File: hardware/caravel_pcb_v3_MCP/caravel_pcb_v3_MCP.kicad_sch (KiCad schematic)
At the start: 38 parts, among them J1 USB_B_Micro - 10118193-0001LF, J2 Conn_01x14_Female, J3 Conn_01x02_Male, J4 Conn_01x02_Male, J5 Conn_01x02_Male, J6 Conn_01x02_Male, J7 Conn_01x06_Female, SW1 SW_Push - SKQGADE010, U1 MCP2221AxML, U2 AZ1117CH-1.8TRG1, U3 AZ1117-3.3, U4 caravel_breakout, U5 W25Q32FVSS, X1 DSC6001_10MHZ

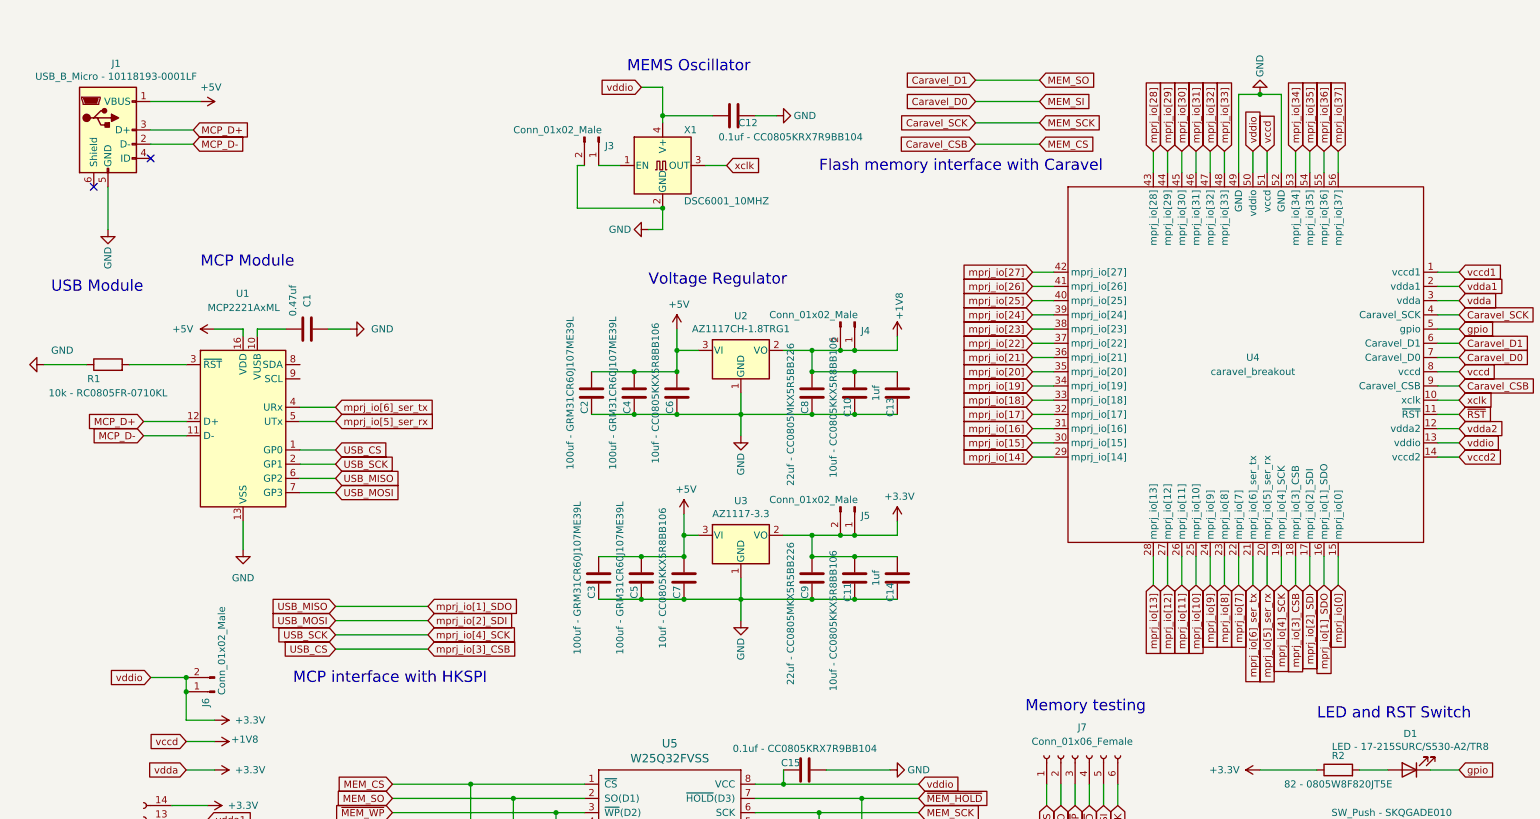
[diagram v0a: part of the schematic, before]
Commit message: Update MCP version of the V3 caravel board
Updates footprint assignments and create initial PCB.

Signed-off-by: Michael Welling <mwelling@ieee.org>
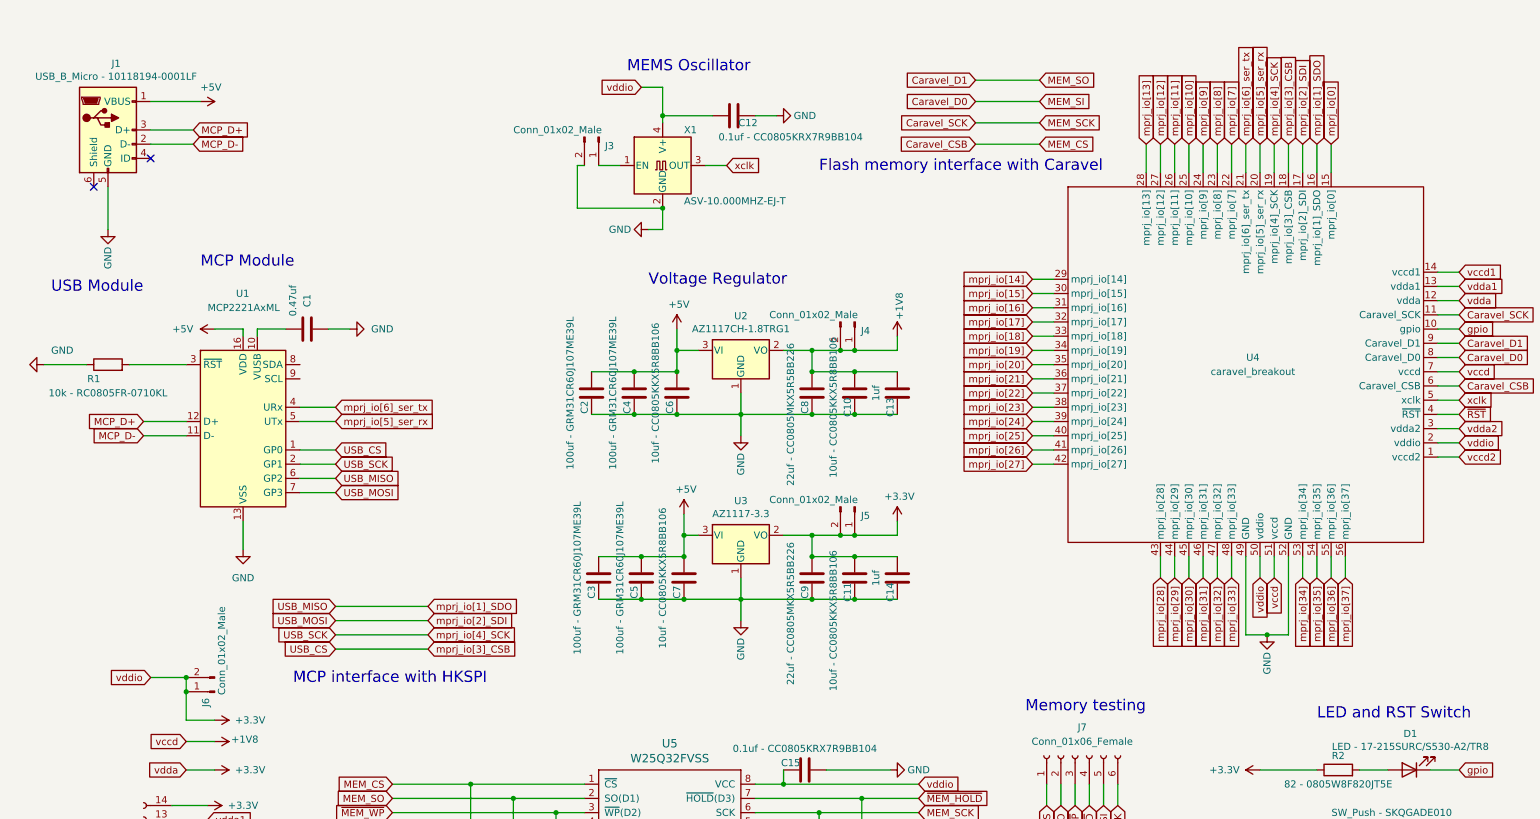
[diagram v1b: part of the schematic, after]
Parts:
- J1: value USB_B_Micro - 10118193-0001LF -> USB_B_Micro - 10118194-0001LF; footprint striVe_foot_prints:FCI_10118193-0001LF -> Connector_USB:USB_Micro-B_Amphenol_10118194_Horizontal
- J7: footprint (none) -> Connector_PinSocket_2.54mm:PinSocket_1x06_P2.54mm_Vertical
- SW1: footprint striVe_foot_prints:SW4-SMD-5.2X5.2X1.5MM -> Button_Switch_SMD:SW_SPST_SKQG_WithStem
- U2, U3: footprint Package_TO_SOT_SMD:SOT-223 -> Package_TO_SOT_SMD:SOT-223-3_TabPin2
- U4: footprint Caravel_Baord:caravel_breakout -> Caravel_Board:caravel_breakout_v1
- U5: footprint striVe_foot_prints:SOIC127P790X216-8N -> Package_SO:SOIC-8_5.23x5.23mm_P1.27mm
- X1: value DSC6001_10MHZ -> ASV-10.000MHZ-EJ-T; footprint striVe_foot_prints:DSC6001JE1A-010.0000 -> Oscillator:Oscillator_SMD_Abracon_ASV-4Pin_7.0x5.1mm
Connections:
- net +1V8: now also U4.7 (vccd); no longer U4.8 (vccd)
- net +3V3: now also U4.12 (vdda), U4.2 (vddio); no longer U4.13 (vddio), U4.3 (vdda)
- net Caravel_CSB: now also U4.6 (Caravel_CSB); no longer U4.9 (Caravel_CSB)
- net Caravel_D0: now also U4.8 (Caravel_D0); no longer U4.7 (Caravel_D0)
- net Caravel_D1: now also U4.9 (Caravel_D1); no longer U4.6 (Caravel_D1)
- net Caravel_SCK: now also U4.11 (Caravel_SCK); no longer U4.4 (Caravel_SCK)
- net gpio: now also U4.10 (gpio); no longer U4.5 (gpio)
- net vccd1: now also U4.14 (vccd1); no longer U4.1 (vccd1)
- net vccd2: now also U4.1 (vccd2); no longer U4.14 (vccd2)
- net vdda1: now also U4.13 (vdda1); no longer U4.2 (vdda1)
- net vdda2: now also U4.3 (vdda2); no longer U4.12 (vdda2)
- net xclk: now also U4.5 (xclk); no longer U4.10 (xclk)
- net ~{RST}: now also U4.4 (~{RST}); no longer U4.11 (~{RST})

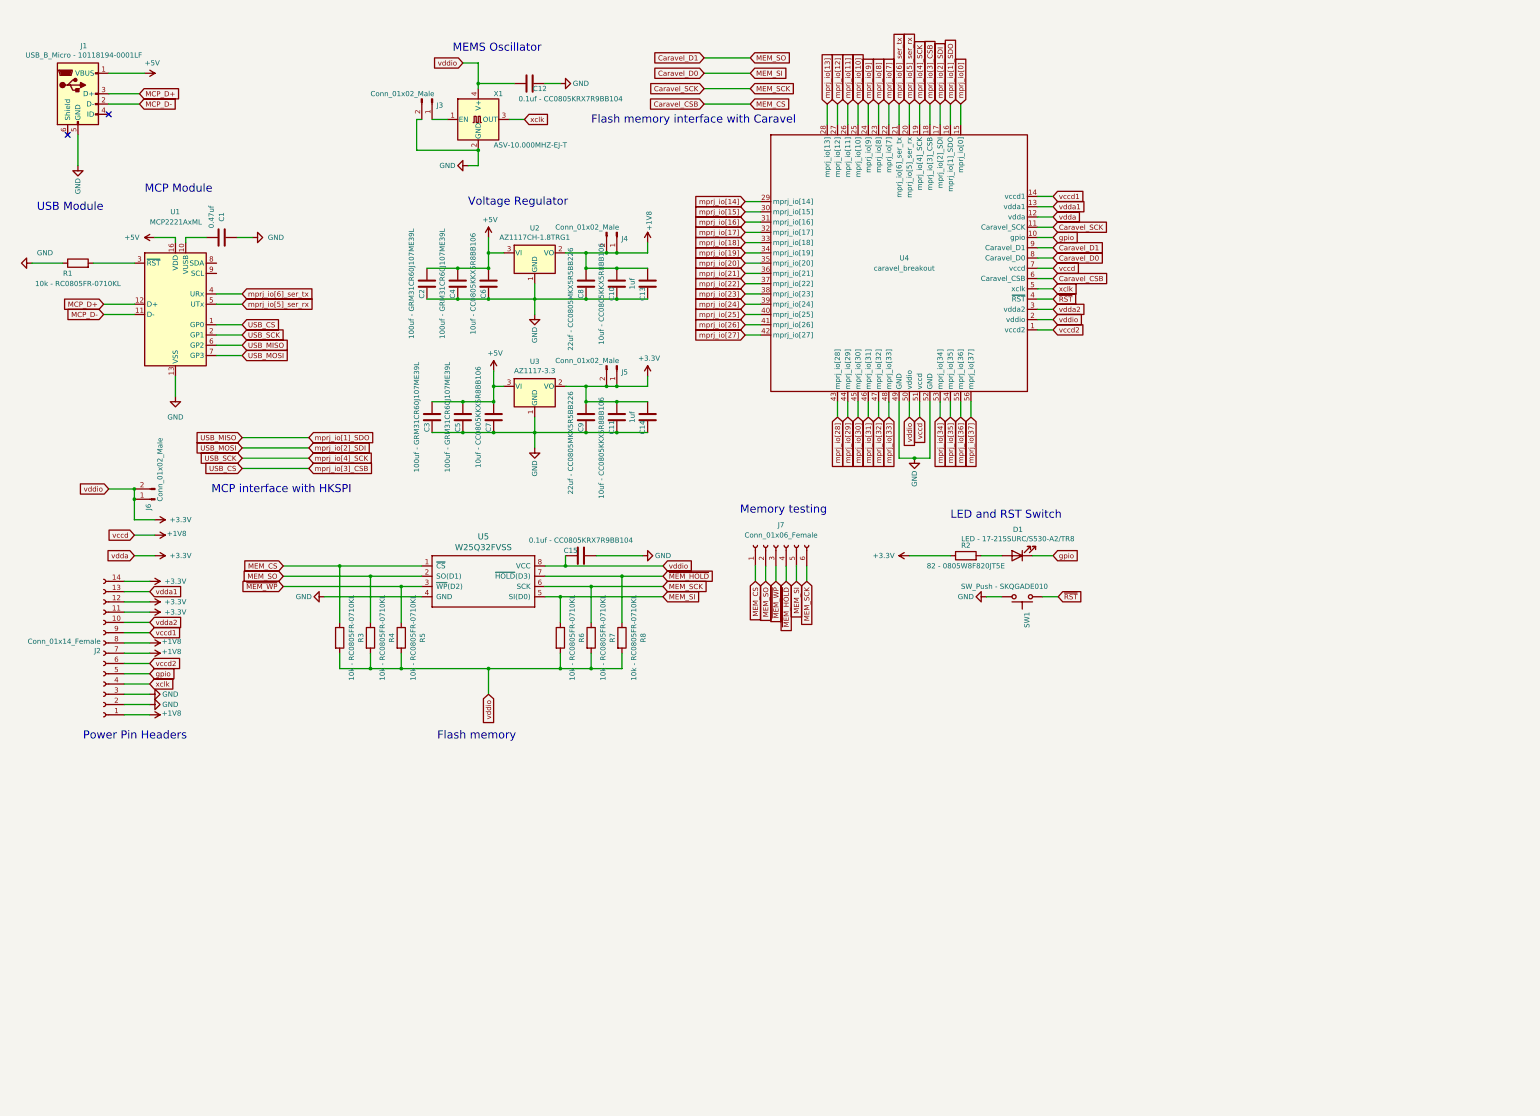
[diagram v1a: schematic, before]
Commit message: update caravel breakout symbol in schematic
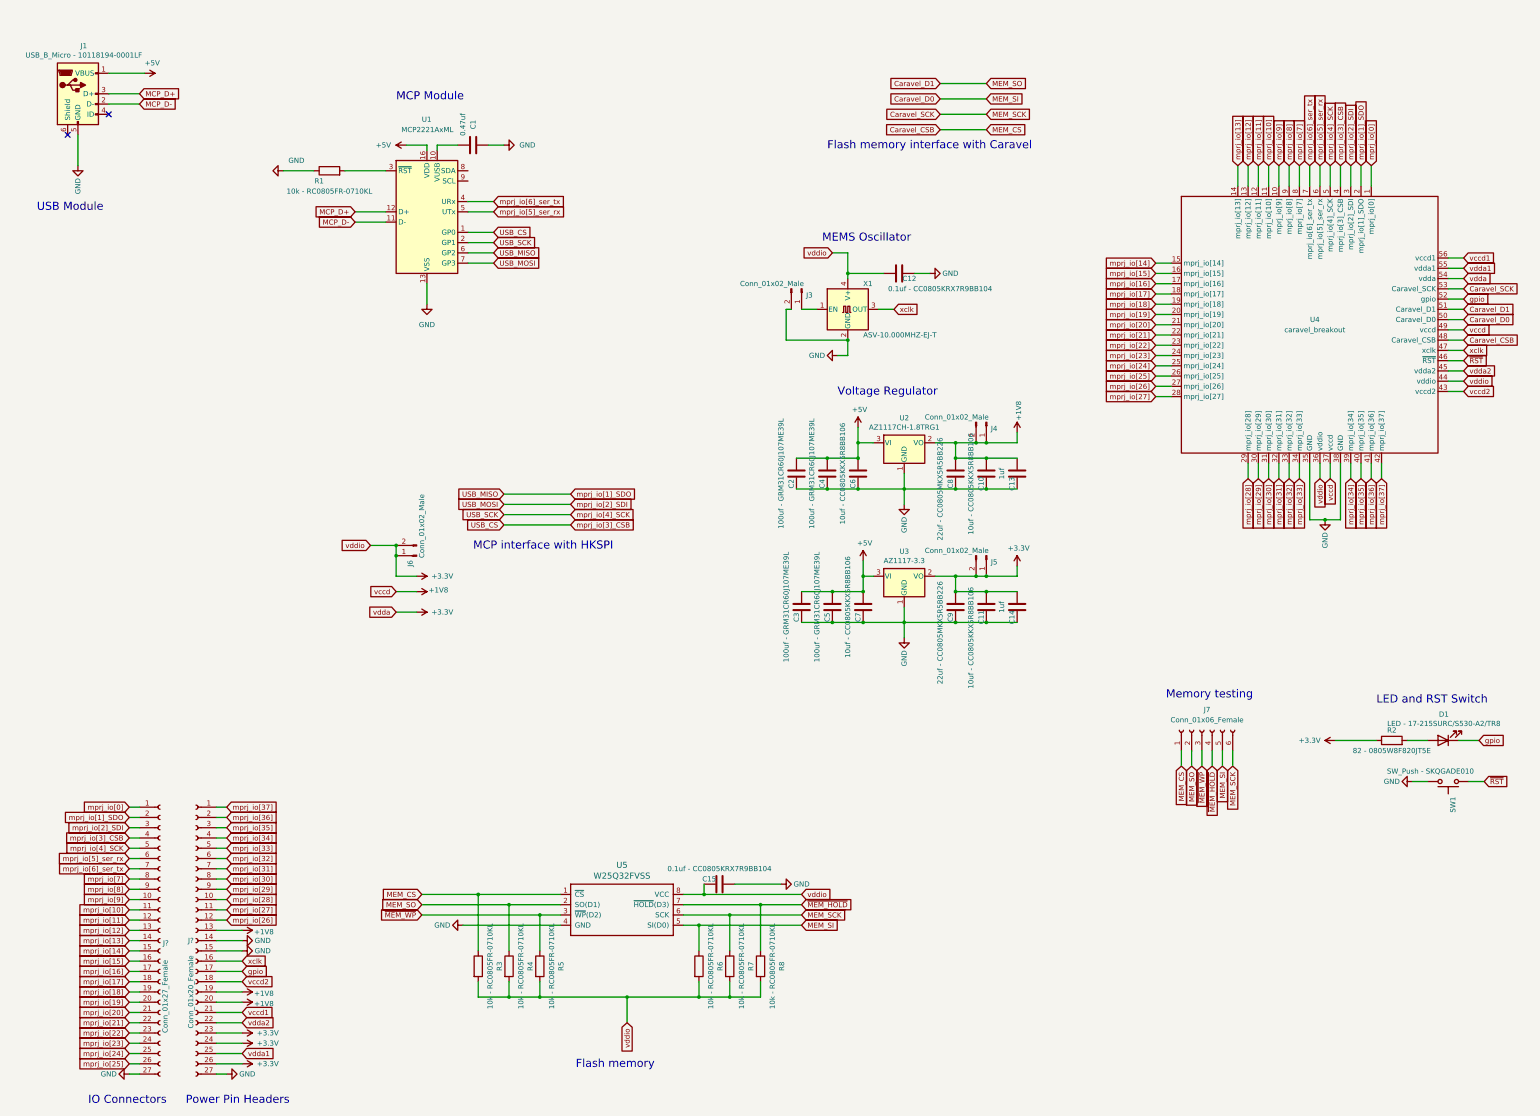
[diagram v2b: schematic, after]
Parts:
- removed J2: Conn_01x14_Female, Connector_PinHeader_2.54mm:PinHeader_1x14_P2.54mm_Vertical, symbol Connector:Conn_01x14_Female
- added J?: Conn_01x27_Female, Connector_PinHeader_2.54mm:PinHeader_1x27_P2.54mm_Vertical, symbol Connector:Conn_01x27_Female
- added J?: Conn_01x20_Female, Connector_PinHeader_2.54mm:PinHeader_1x20_P2.54mm_Vertical, symbol Connector:Conn_01x27_Female
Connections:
- net +1V8: now also U4.37 (vccd), U4.49 (vccd), J?.13 (Pin_13), J?.19 (Pin_19), J?.20 (Pin_20); no longer U4.51 (vccd), U4.7 (vccd)
- net +3V3: now also U4.36 (vddio), U4.44 (vddio), U4.54 (vdda), J?.23 (Pin_23), J?.24 (Pin_24), J?.26 (Pin_26); no longer U4.12 (vdda), U4.2 (vddio), U4.50 (vddio)
- net Caravel_CSB: now also U4.48 (Caravel_CSB); no longer U4.6 (Caravel_CSB)
- net Caravel_D0: now also U4.50 (Caravel_D0); no longer U4.8 (Caravel_D0)
- net Caravel_D1: now also U4.51 (Caravel_D1); no longer U4.9 (Caravel_D1)
- net Caravel_SCK: now also U4.53 (Caravel_SCK); no longer U4.11 (Caravel_SCK)
- net GND: now also U4.35 (GND), U4.38 (GND), J?.14 (Pin_14), J?.15 (Pin_15), J?.27 (Pin_27), J?.27 (Pin_27); no longer U4.49 (GND), U4.52 (GND)
- net USB_CS: now also U4.4 (mprj_io[3]_CSB), J?.4 (Pin_4); no longer U4.18 (mprj_io[3]_CSB)
- net USB_MISO: now also U4.2 (mprj_io[1]_SDO), J?.2 (Pin_2); no longer U4.16 (mprj_io[1]_SDO)
- net USB_MOSI: now also U4.3 (mprj_io[2]_SDI), J?.3 (Pin_3); no longer U4.17 (mprj_io[2]_SDI)
- net USB_SCK: now also U4.5 (mprj_io[4]_SCK), J?.5 (Pin_5); no longer U4.19 (mprj_io[4]_SCK)
- net gpio: now also U4.52 (gpio), J?.17 (Pin_17); no longer U4.10 (gpio)
- net mprj_io[0]: now also U4.1 (mprj_io[0]), J?.1 (Pin_1); no longer U4.15 (mprj_io[0])
- net mprj_io[10]: now also U4.11 (mprj_io[10]), J?.11 (Pin_11); no longer U4.25 (mprj_io[10])
- net mprj_io[11]: now also U4.12 (mprj_io[11]), J?.12 (Pin_12); no longer U4.26 (mprj_io[11])
- net mprj_io[12]: now also U4.13 (mprj_io[12]), J?.13 (Pin_13); no longer U4.27 (mprj_io[12])
- net mprj_io[13]: now also U4.14 (mprj_io[13]), J?.14 (Pin_14); no longer U4.28 (mprj_io[13])
- net mprj_io[14]: now also U4.15 (mprj_io[14]), J?.15 (Pin_15); no longer U4.29 (mprj_io[14])
- net mprj_io[15]: now also U4.16 (mprj_io[15]), J?.16 (Pin_16); no longer U4.30 (mprj_io[15])
- net mprj_io[16]: now also U4.17 (mprj_io[16]), J?.17 (Pin_17); no longer U4.31 (mprj_io[16])
- net mprj_io[17]: now also U4.18 (mprj_io[17]), J?.18 (Pin_18); no longer U4.32 (mprj_io[17])
- net mprj_io[18]: now also U4.19 (mprj_io[18]), J?.19 (Pin_19); no longer U4.33 (mprj_io[18])
- net mprj_io[19]: now also U4.20 (mprj_io[19]), J?.20 (Pin_20); no longer U4.34 (mprj_io[19])
- net mprj_io[20]: now also U4.21 (mprj_io[20]), J?.21 (Pin_21); no longer U4.35 (mprj_io[20])
- net mprj_io[21]: now also U4.22 (mprj_io[21]), J?.22 (Pin_22); no longer U4.36 (mprj_io[21])
- net mprj_io[22]: now also U4.23 (mprj_io[22]), J?.23 (Pin_23); no longer U4.37 (mprj_io[22])
- net mprj_io[23]: now also U4.24 (mprj_io[23]), J?.24 (Pin_24); no longer U4.38 (mprj_io[23])
- net mprj_io[24]: now also U4.25 (mprj_io[24]), J?.25 (Pin_25); no longer U4.39 (mprj_io[24])
- net mprj_io[25]: now also U4.26 (mprj_io[25]), J?.26 (Pin_26); no longer U4.40 (mprj_io[25])
- net mprj_io[26]: now also U4.27 (mprj_io[26]), J?.12 (Pin_12); no longer U4.41 (mprj_io[26])
- net mprj_io[27]: now also U4.28 (mprj_io[27]), J?.11 (Pin_11); no longer U4.42 (mprj_io[27])
- net mprj_io[28]: now also U4.29 (mprj_io[28]), J?.10 (Pin_10); no longer U4.43 (mprj_io[28])
- net mprj_io[29]: now also U4.30 (mprj_io[29]), J?.9 (Pin_9); no longer U4.44 (mprj_io[29])
- net mprj_io[30]: now also U4.31 (mprj_io[30]), J?.8 (Pin_8); no longer U4.45 (mprj_io[30])
- net mprj_io[31]: now also U4.32 (mprj_io[31]), J?.7 (Pin_7); no longer U4.46 (mprj_io[31])
- net mprj_io[32]: now also U4.33 (mprj_io[32]), J?.6 (Pin_6); no longer U4.47 (mprj_io[32])
- net mprj_io[33]: now also U4.34 (mprj_io[33]), J?.5 (Pin_5); no longer U4.48 (mprj_io[33])
- net mprj_io[34]: now also U4.39 (mprj_io[34]), J?.4 (Pin_4); no longer U4.53 (mprj_io[34])
- net mprj_io[35]: now also U4.40 (mprj_io[35]), J?.3 (Pin_3); no longer U4.54 (mprj_io[35])
- net mprj_io[36]: now also U4.41 (mprj_io[36]), J?.2 (Pin_2); no longer U4.55 (mprj_io[36])
- net mprj_io[37]: now also U4.42 (mprj_io[37]), J?.1 (Pin_1); no longer U4.56 (mprj_io[37])
- net mprj_io[5]_ser_rx: now also U4.6 (mprj_io[5]_ser_rx), J?.6 (Pin_6); no longer U4.20 (mprj_io[5]_ser_rx)
- net mprj_io[6]_ser_tx: now also U4.7 (mprj_io[6]_ser_tx), J?.7 (Pin_7); no longer U4.21 (mprj_io[6]_ser_tx)
- net mprj_io[7]: now also U4.8 (mprj_io[7]), J?.8 (Pin_8); no longer U4.22 (mprj_io[7])
- net mprj_io[8]: now also U4.9 (mprj_io[8]), J?.9 (Pin_9); no longer U4.23 (mprj_io[8])
- net mprj_io[9]: now also U4.10 (mprj_io[9]), J?.10 (Pin_10); no longer U4.24 (mprj_io[9])
- net vccd1: now also U4.56 (vccd1), J?.21 (Pin_21); no longer U4.14 (vccd1)
- net vccd2: now also U4.43 (vccd2), J?.18 (Pin_18); no longer U4.1 (vccd2)
- net vdda1: now also U4.55 (vdda1), J?.25 (Pin_25); no longer U4.13 (vdda1)
- net vdda2: now also U4.45 (vdda2), J?.22 (Pin_22); no longer U4.3 (vdda2)
- net xclk: now also U4.47 (xclk), J?.16 (Pin_16); no longer U4.5 (xclk)
- net ~{RST}: now also U4.46 (~{RST}); no longer U4.4 (~{RST})
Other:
- note added: "IO Connectors"
- moved on the sheet: C1, C10, C11, C12, C13, C14, C15, C2, C3, C4, C5, C6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
